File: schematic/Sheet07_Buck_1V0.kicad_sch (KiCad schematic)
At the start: 14 parts, among them U5 TPS7H5001-SP

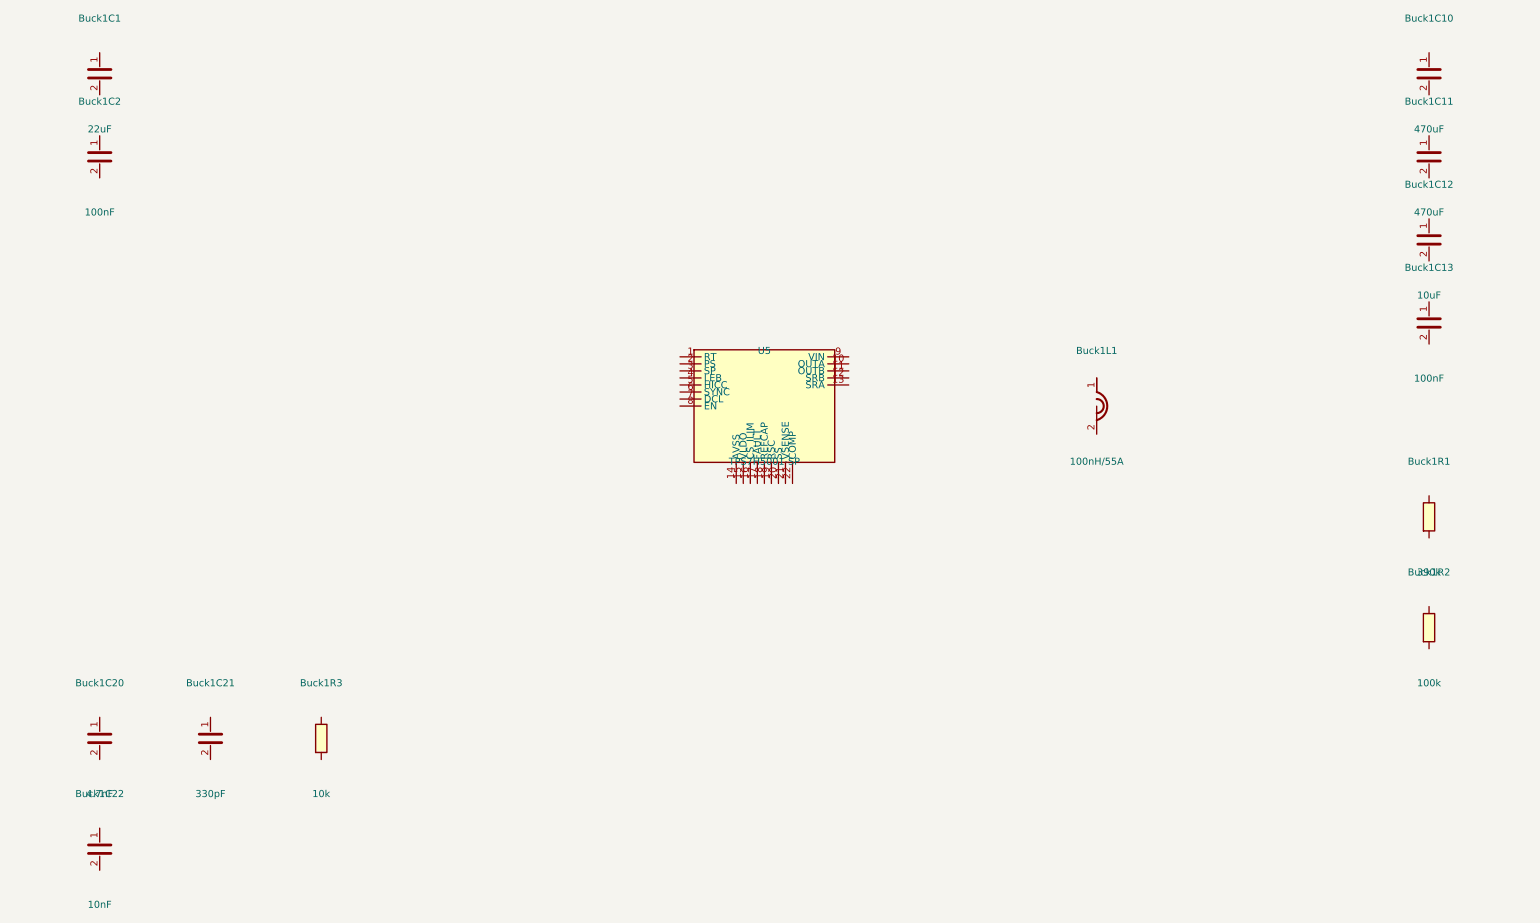
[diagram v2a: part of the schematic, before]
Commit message: feat: add 745 wire connections linking all IC pins to labels and power symbols
- Added stub wires from every component pin to net labels/global_labels
- Power pins connected to correct power symbols (GND, +1V0, +1V8, +3V3, etc.)
- Signal pins connected to labeled nets matching design spec
- Global labels for cross-sheet signals (JESD, SPI, clock, SpaceWire)
- Fixed missing +3V3 power symbol definitions in 5 sheets
- All 17 sheets export successfully with KiCad CLI (17/17 OK)
- Merged PDF: 3.1MB, 17 pages with visible wire connections
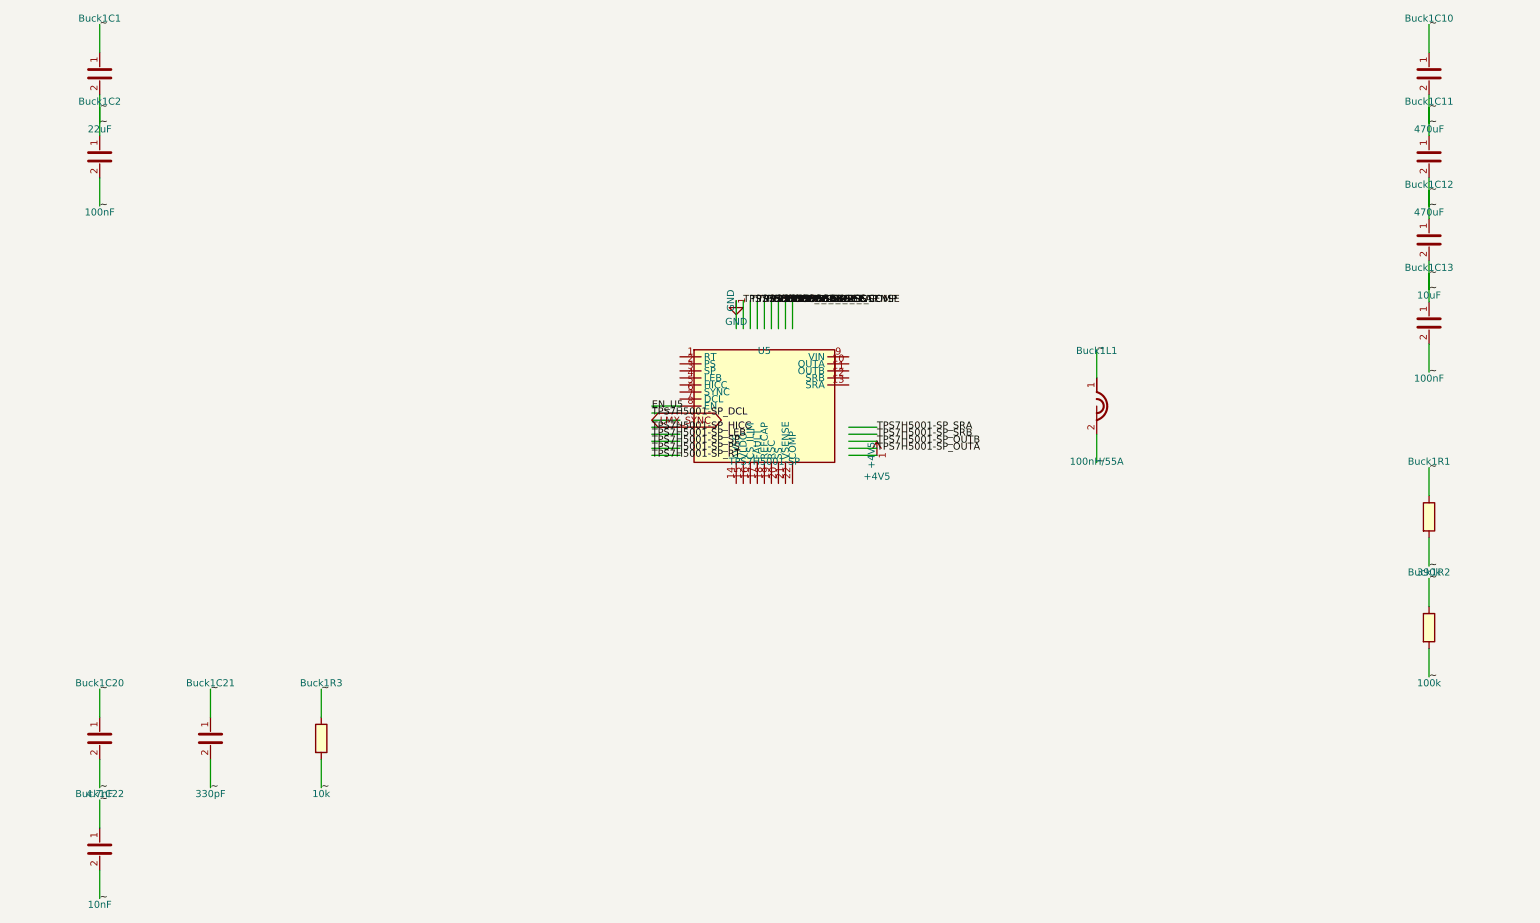
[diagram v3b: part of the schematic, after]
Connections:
- net ~: now reaches Buck1R1.1
- net ~: now also Buck1C1.1, Buck1C1.2, Buck1C10.1, Buck1C10.2, Buck1C11.1, Buck1C11.2, Buck1C12.1, Buck1C12.2, Buck1C13.1, Buck1C13.2, Buck1C2.1, Buck1C2.2, Buck1C20.1, Buck1C20.2, Buck1C21.1, Buck1C21.2, Buck1C22.1, Buck1C22.2, Buck1L1.1, Buck1L1.2, Buck1R1.2, Buck1R2.1, Buck1R2.2, Buck1R3.1, Buck1R3.2
- net EN_U5: now reaches U5.8 (EN)
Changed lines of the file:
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@@
     (pin "1")
     (pin "2")
-  )  (global_label "VIN_4V5" (shape input) (at 60 60 180) (effects (font (size 1.27 1.27)) (justify right)))  (global_label "VCCINT_1V0" (shape output) (at 400 60 0) (effects (font (size 1.27 1.27)) (justify left)))  (global_label "BUCK1_EN" (shape input) (at 60 180 180) (effects (font (size 1.27 1.27)) (justify right)))  (global_label "BUCK1_PG" (shape output) (at 400 120 0) (effects (font (size 1.27 1.27)) (justify left)))  (sheet_instances (path "/" (page "1")))
+  )  (global_label "VIN_4V5" (shape input) (at 60 60 180) (effects (font (size 1.27 1.27)) (justify right)))  (global_label "VCCINT_1V0" (shape output) (at 400 60 0) (effects (font (size 1.27 1.27)) (justify left)))  (global_label "BUCK1_EN" (shape input) (at 60 180 180) (effects (font (size 1.27 1.27)) (justify right)))  (global_label "BUCK1_PG" (shape output) (at 400 120 0) (effects (font (size 1.27 1.27)) (justify left)))
+  (wire (pts (xy 184.76 108.89) (xy 179.68 108.89)) (stroke (width 0) (type default)))
+  (label "TPS7H5001-SP_RT" (at 179.68 108.89 0) (effects (font (size 1.27 1.27))))
+  (wire (pts (xy 184.76 107.62) (xy 179.68 107.62)) (stroke (width 0) (type default)))
+  (label "TPS7H5001-SP_PS" (at 179.68 107.62 0) (effects (font (size 1.27 1.27))))
+  (wire (pts (xy 184.76 106.35) (xy 179.68 106.35)) (stroke (width 0) (type default)))
+  (label "TPS7H5001-SP_SP" (at 179.68 106.35 0) (effects (font (size 1.27 1.27))))
+  (wire (pts (xy 184.76 105.08) (xy 179.68 105.08)) (stroke (width 0) (type default)))
+  (label "TPS7H5001-SP_LEB" (at 179.68 105.08 0) (effects (font (size 1.27 1.27))))
+  (wire (pts (xy 184.76 103.81) (xy 179.68 103.81)) (stroke (width 0) (type default)))
+  (label "TPS7H5001-SP_HICC" (at 179.68 103.81 0) (effects (font (size 1.27 1.27))))
+  (wire (pts (xy 184.76 102.54) (xy 179.68 102.54)) (stroke (width 0) (type default)))
+  (global_label "LMX_SYNC" (shape bidirectional) (at 179.68 102.54 0) (effects (font (size 1.27 1.27)) (justify left)))
+  (wire (pts (xy 184.76 101.27) (xy 179.68 101.27)) (stroke (width 0) (type default)))
+  (label "TPS7H5001-SP_DCL" (at 179.68 101.27 0) (effects (font (size 1.27 1.27))))
+  (wire (pts (xy 184.76 100.00) (xy 179.68 100.00)) (stroke (width 0) (type default)))
+  (label "EN_U5" (at 179.68 100.00 0) (effects (font (size 1.27 1.27))))
+  (wire (pts (xy 215.24 108.89) (xy 220.32 108.89)) (stroke (width 0) (type default)))
+  (symbol (lib_id "power:+4V5") (at 220.32 108.89 0) (unit 1)
+      (in_bom yes) (on_board yes) (dnp no)
+      (property "Reference" "#PWR6bb" (at 220.32 105.08 0) (effects (font (size 1.27 1.27)) hide))
+      (property "Value" "+4V5" (at 220.32 112.70 0) (effects (font (size 1.27 1.27))))
+      (property "Footprint" "" (at 0 0 0) (effects (font (size 1.27 1.27)) hide))
+      (property "Datasheet" "" (at 0 0 0) (effects (font (size 1.27 1.27)) hide))
+      (pin "1")
+    )
+  (wire (pts (xy 215.24 107.62) (xy 220.32 107.62)) (stroke (width 0) (type default)))
+  (label "TPS7H5001-SP_OUTA" (at 220.32 107.62 0) (effects (font (size 1.27 1.27))))
+  (wire (pts (xy 215.24 106.35) (xy 220.32 106.35)) (stroke (width 0) (type default)))
+  (label "TPS7H5001-SP_OUTB" (at 220.32 106.35 0) (effects (font (size 1.27 1.27))))
+  (wire (pts (xy 215.24 105.08) (xy 220.32 105.08)) (stroke (width 0) (type default)))
+  (label "TPS7H5001-SP_SRB" (at 220.32 105.08 0) (effects (font (size 1.27 1.27))))
+  (wire (pts (xy 215.24 103.81) (xy 220.32 103.81)) (stroke (width 0) (type default)))
+  (label "TPS7H5001-SP_SRA" (at 220.32 103.81 0) (effects (font (size 1.27 1.27))))
+  (wire (pts (xy 194.92 86.03) (xy 194.92 80.95)) (stroke (width 0) (type default)))
+  (symbol (lib_id "power:GND") (at 194.92 80.95 0) (unit 1)
+      (in_bom yes) (on_board yes) (dnp no)
+      (property "Reference" "#PWR5c6" (at 194.92 77.14 0) (effects (font (size 1.27 1.27)) hide))
+      (property "Value" "GND" (at 194.92 84.76 0) (effects (font (size 1.27 1.27))))
+      (property "Footprint" "" (at 0 0 0) (effects (font (size 1.27 1.27)) hide))
+      (property "Datasheet" "" (at 0 0 0) (effects (font (size 1.27 1.27)) hide))
+      (pin "1")
+    )
+  (wire (pts (xy 196.19 86.03) (xy 196.19 80.95)) (stroke (width 0) (type default)))
+  (label "TPS7H5001-SP_VLDO" (at 196.19 80.95 0) (effects (font (size 1.27 1.27))))
+  (wire (pts (xy 197.46 86.03) (xy 197.46 80.95)) (stroke (width 0) (type default)))
+  (label "TPS7H5001-SP_CS" (at 197.46 80.95 0) (effects (font (size 1.27 1.27))))
+  (wire (pts (xy 198.73 86.03) (xy 198.73 80.95)) (stroke (width 0) (type default)))
+  (label "TPS7H5001-SP_FAULT" (at 198.73 80.95 0) (effects (font (size 1.27 1.27))))
+  (wire (pts (xy 200.00 86.03) (xy 200.00 80.95)) (stroke (width 0) (type default)))
+  (label "TPS7H5001-SP_REFCAP" (at 200.00 80.95 0) (effects (font (size 1.27 1.27))))
+  (wire (pts (xy 201.27 86.03) (xy 201.27 80.95)) (stroke (width 0) (type default)))
+  (label "TPS7H5001-SP_RSC" (at 201.27 80.95 0) (effects (font (size 1.27 1.27))))
+  (wire (pts (xy 202.54 86.03) (xy 202.54 80.95)) (stroke (width 0) (type default)))
+  (label "TPS7H5001-SP_SS" (at 202.54 80.95 0) (effects (font (size 1.27 1.27))))
+  (wire (pts (xy 203.81 86.03) (xy 203.81 80.95)) (stroke (width 0) (type default)))
+  (label "TPS7H5001-SP_VSENSE" (at 203.81 80.95 0) (effects (font (size 1.27 1.27))))
+  (wire (pts (xy 205.08 86.03) (xy 205.08 80.95)) (stroke (width 0) (type default)))
+  (label "TPS7H5001-SP_COMP" (at 205.08 80.95 0) (effects (font (size 1.27 1.27))))
+  (wire (pts (xy 80.00 43.81) (xy 80.00 48.89)) (stroke (width 0) (type default)))
+  (label "~" (at 80.00 48.89 0) (effects (font (size 1.27 1.27))))
+  (wire (pts (xy 80.00 36.19) (xy 80.00 31.11)) (stroke (width 0) (type default)))
+  (label "~" (at 80.00 31.11 0) (effects (font (size 1.27 1.27))))
+  (wire (pts (xy 80.00 58.81) (xy 80.00 63.89)) (stroke (width 0) (type default)))
+  (label "~" (at 80.00 63.89 0) (effects (font (size 1.27 1.27))))
+  (wire (pts (xy 80.00 51.19) (xy 80.00 46.11)) (stroke (width 0) (type default)))
+  (label "~" (at 80.00 46.11 0) (effects (font (size 1.27 1.27))))
+  (wire (pts (xy 320.00 43.81) (xy 320.00 48.89)) (stroke (width 0) (type default)))
+  (label "~" (at 320.00 48.89 0) (effects (font (size 1.27 1.27))))
+  (wire (pts (xy 320.00 36.19) (xy 320.00 31.11)) (stroke (width 0) (type default)))
+  (label "~" (at 320.00 31.11 0) (effects (font (size 1.27 1.27))))
+  (wire (pts (xy 320.00 58.81) (xy 320.00 63.89)) (stroke (width 0) (type default)))
+  (label "~" (at 320.00 63.89 0) (effects (font (size 1.27 1.27))))
+  (wire (pts (xy 320.00 51.19) (xy 320.00 46.11)) (stroke (width 0) (type default)))
+  (label "~" (at 320.00 46.11 0) (effects (font (size 1.27 1.27))))
+  (wire (pts (xy 320.00 73.81) (xy 320.00 78.89)) (stroke (width 0) (type default)))
+  (label "~" (at 320.00 78.89 0) (effects (font (size 1.27 1.27))))
+  (wire (pts (xy 320.00 66.19) (xy 320.00 61.11)) (stroke (width 0) (type default)))
+  (label "~" (at 320.00 61.11 0) (effects (font (size 1.27 1.27))))
+  (wire (pts (xy 320.00 88.81) (xy 320.00 93.89)) (stroke (width 0) (type default)))
+  (label "~" (at 320.00 93.89 0) (effects (font (size 1.27 1.27))))
+  (wire (pts (xy 320.00 81.19) (xy 320.00 76.11)) (stroke (width 0) (type default)))
+  (label "~" (at 320.00 76.11 0) (effects (font (size 1.27 1.27))))
+  (wire (pts (xy 260.00 105.08) (xy 260.00 110.16)) (stroke (width 0) (type default)))
+  (label "~" (at 260.00 110.16 0) (effects (font (size 1.27 1.27))))
+  (wire (pts (xy 260.00 94.92) (xy 260.00 89.84)) (stroke (width 0) (type default)))
+  (label "~" (at 260.00 89.84 0) (effects (font (size 1.27 1.27))))
+  (wire (pts (xy 320.00 123.81) (xy 320.00 128.89)) (stroke (width 0) (type default)))
+  (label "~" (at 320.00 128.89 0) (effects (font (size 1.27 1.27))))
+  (wire (pts (xy 320.00 116.19) (xy 320.00 111.11)) (stroke (width 0) (type default)))
+  (label "~" (at 320.00 111.11 0) (effects (font (size 1.27 1.27))))
+  (wire (pts (xy 320.00 143.81) (xy 320.00 148.89)) (stroke (width 0) (type default)))
+  (label "~" (at 320.00 148.89 0) (effects (font (size 1.27 1.27))))
+  (wire (pts (xy 320.00 136.19) (xy 320.00 131.11)) (stroke (width 0) (type default)))
+  (label "~" (at 320.00 131.11 0) (effects (font (size 1.27 1.27))))
+  (wire (pts (xy 80.00 163.81) (xy 80.00 168.89)) (stroke (width 0) (type default)))
+  (label "~" (at 80.00 168.89 0) (effects (font (size 1.27 1.27))))
+  (wire (pts (xy 80.00 156.19) (xy 80.00 151.11)) (stroke (width 0) (type default)))
+  (label "~" (at 80.00 151.11 0) (effects (font (size 1.27 1.27))))
+  (wire (pts (xy 100.00 163.81) (xy 100.00 168.89)) (stroke (width 0) (type default)))
+  (label "~" (at 100.00 168.89 0) (effects (font (size 1.27 1.27))))
+  (wire (pts (xy 100.00 156.19) (xy 100.00 151.11)) (stroke (width 0) (type default)))
+  (label "~" (at 100.00 151.11 0) (effects (font (size 1.27 1.27))))
+  (wire (pts (xy 120.00 163.81) (xy 120.00 168.89)) (stroke (width 0) (type default)))
+  (label "~" (at 120.00 168.89 0) (effects (font (size 1.27 1.27))))
+  (wire (pts (xy 120.00 156.19) (xy 120.00 151.11)) (stroke (width 0) (type default)))
+  (label "~" (at 120.00 151.11 0) (effects (font (size 1.27 1.27))))
+  (wire (pts (xy 80.00 183.81) (xy 80.00 188.89)) (stroke (width 0) (type default)))
+  (label "~" (at 80.00 188.89 0) (effects (font (size 1.27 1.27))))
+  (wire (pts (xy 80.00 176.19) (xy 80.00 171.11)) (stroke (width 0) (type default)))
+  (label "~" (at 80.00 171.11 0) (effects (font (size 1.27 1.27))))
+  (sheet_instances (path "/" (page "1")))
 )

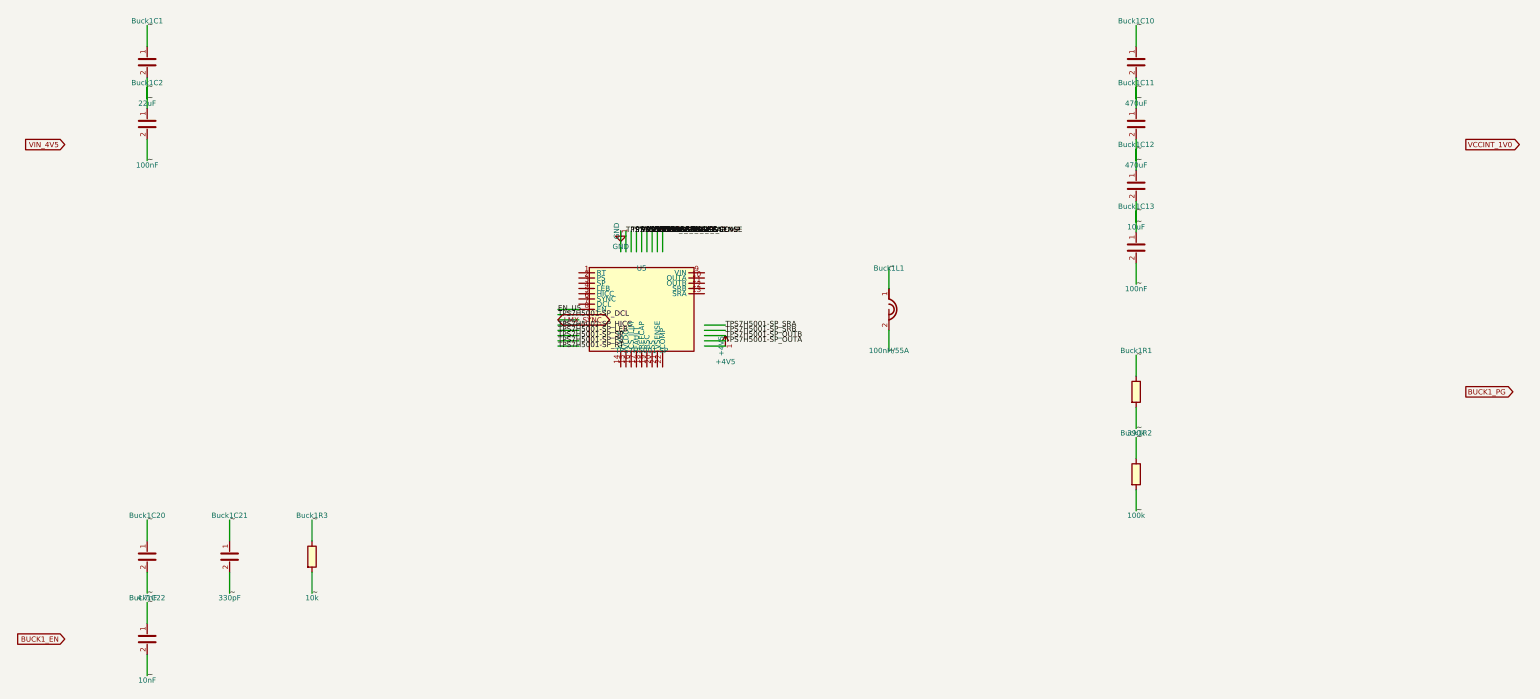
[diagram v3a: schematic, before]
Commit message: Fix KiCad schematic wiring: Y-inversion bug + all 891 pins connected
- Fixed critical Y-axis inversion bug: KiCad inverts Y when placing
  symbols (lib Y + schematic Y = abs Y is WRONG; correct: abs Y = sym Y - lib Y)
- This caused ALL wires to connect to wrong pins (e.g., CS label connected
  to BG pin instead of CS pin)
- Verified with netlist: 0 unconnected nets, all pin functions correct
- Fixed wire direction for angle 90/270 (swapped due to Y-inversion)
- 891 pin connections across 15 sheets, all 17 sheets export without errors
- Netlist verification: CS→E8, BG→C3, INA+→A4, CLK+→F1, JESD pairs correct

Co-Authored-By: opencode <noreply@opencode.ai>
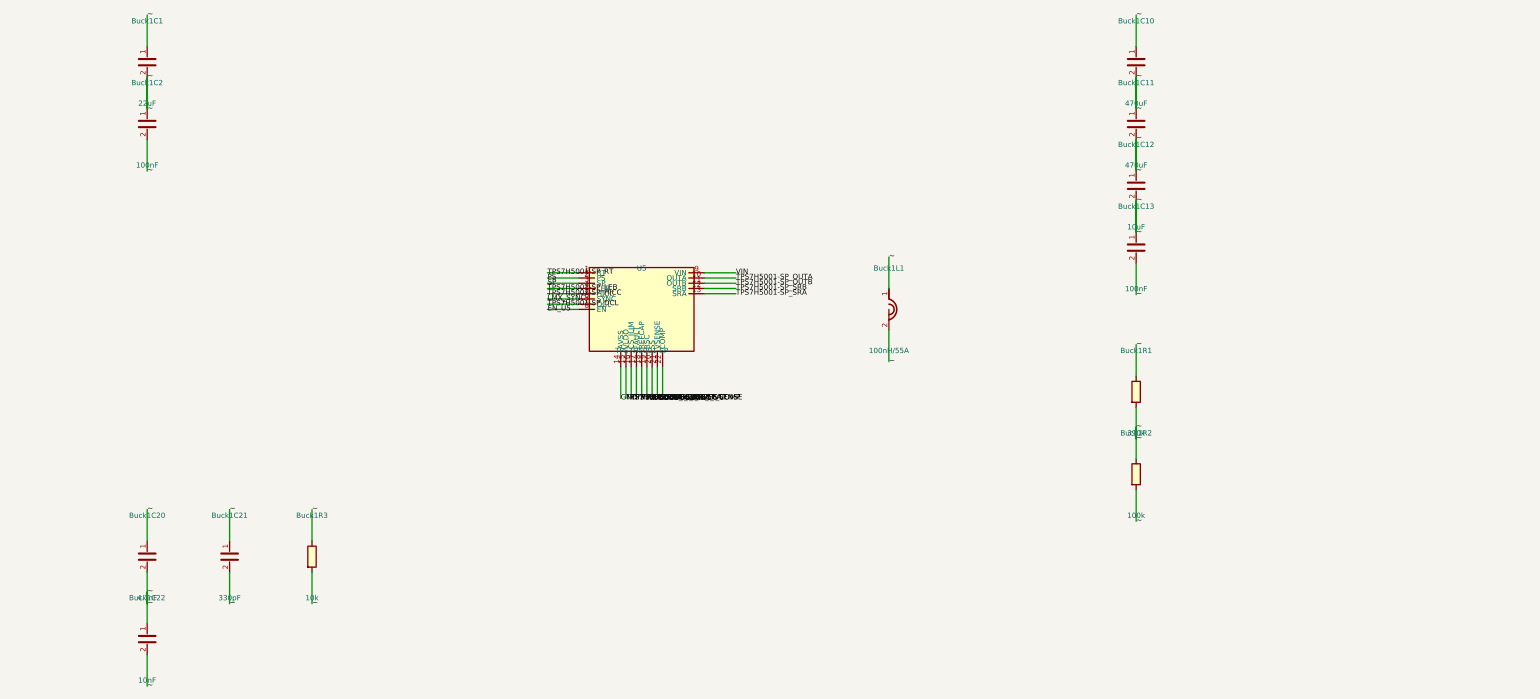
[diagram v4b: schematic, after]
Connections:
- net GND: now also U5.14 (AVSS)
- net LMX_SYNC: now also U5.6 (SYNC)
- net TPS7H5001-SP_COMP: now also U5.22 (COMP)
- net TPS7H5001-SP_CS: now also U5.16 (CS_ILIM)
- net TPS7H5001-SP_DCL: now also U5.7 (DCL)
- net TPS7H5001-SP_FAULT: now also U5.17 (FAULT)
- net TPS7H5001-SP_HICC: now also U5.5 (HICC)
- net TPS7H5001-SP_LEB: now also U5.4 (LEB)
- net TPS7H5001-SP_OUTA: now also U5.10 (OUTA)
- net TPS7H5001-SP_OUTB: now also U5.11 (OUTB)
- net TPS7H5001-SP_REFCAP: now also U5.18 (REFCAP)
- net TPS7H5001-SP_RT: now also U5.1 (RT)
- net TPS7H5001-SP_SRA: now also U5.13 (SRA)
- net TPS7H5001-SP_SRB: now also U5.12 (SRB)
- net TPS7H5001-SP_SS: now also U5.20 (SS)
- net TPS7H5001-SP_VLDO: now also U5.15 (VLDO)
- net TPS7H5001-SP_VSENSE: now also U5.21 (VSENSE)
- net RSC: now reaches U5.19 (RSC)
- net PS: now reaches U5.2 (PS)
- net SP: now reaches U5.3 (SP)
- net VIN: now reaches U5.9 (VIN)
